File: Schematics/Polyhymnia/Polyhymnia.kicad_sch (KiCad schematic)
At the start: 1 part, among them U1 Teensy4.1

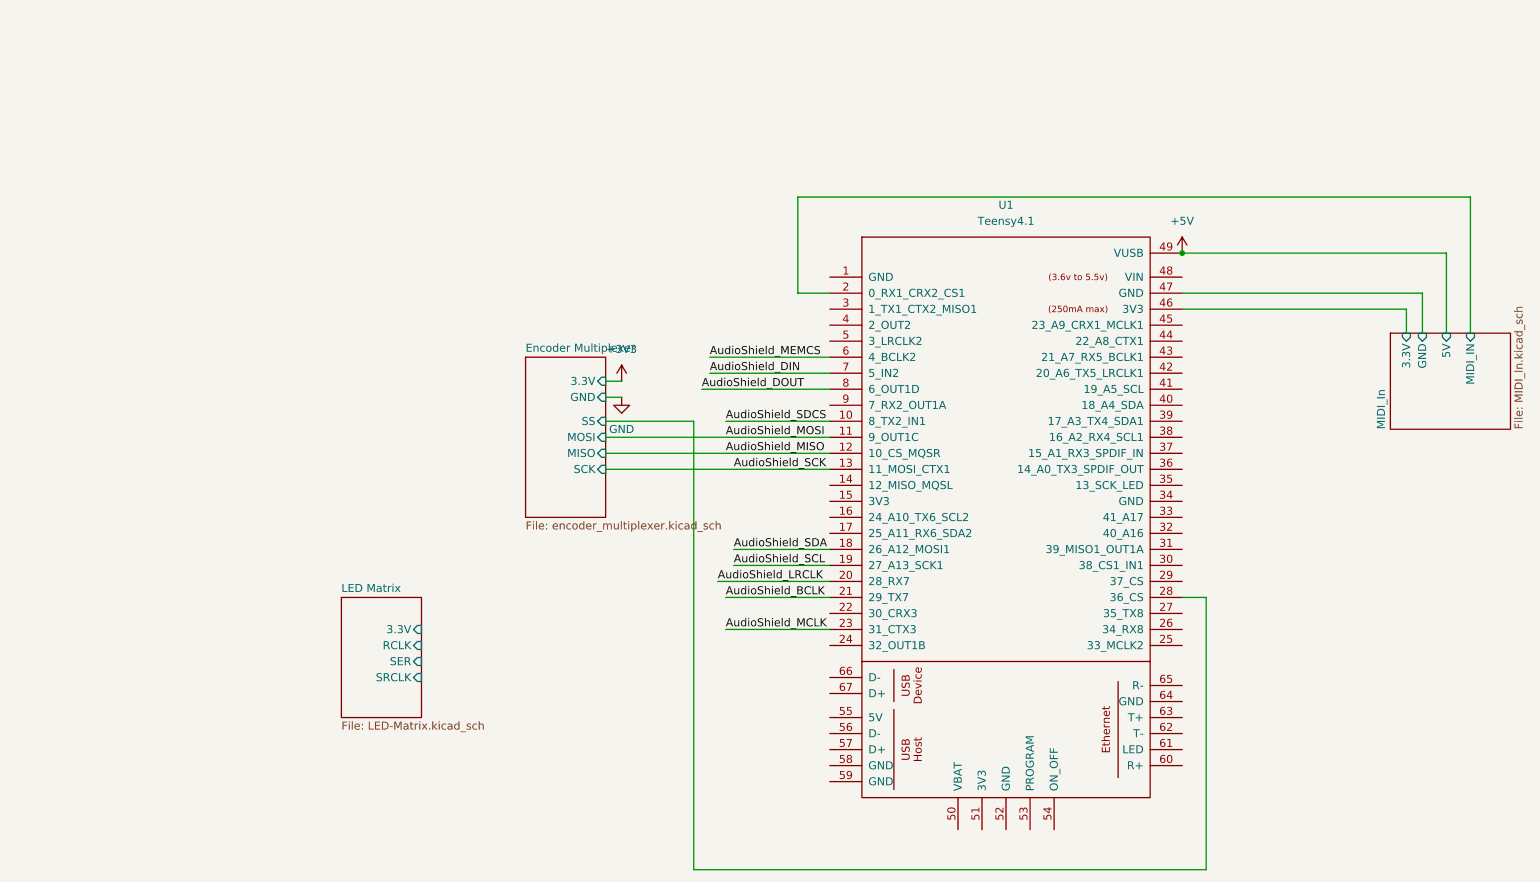
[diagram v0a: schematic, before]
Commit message: Added audio amplifier schematics
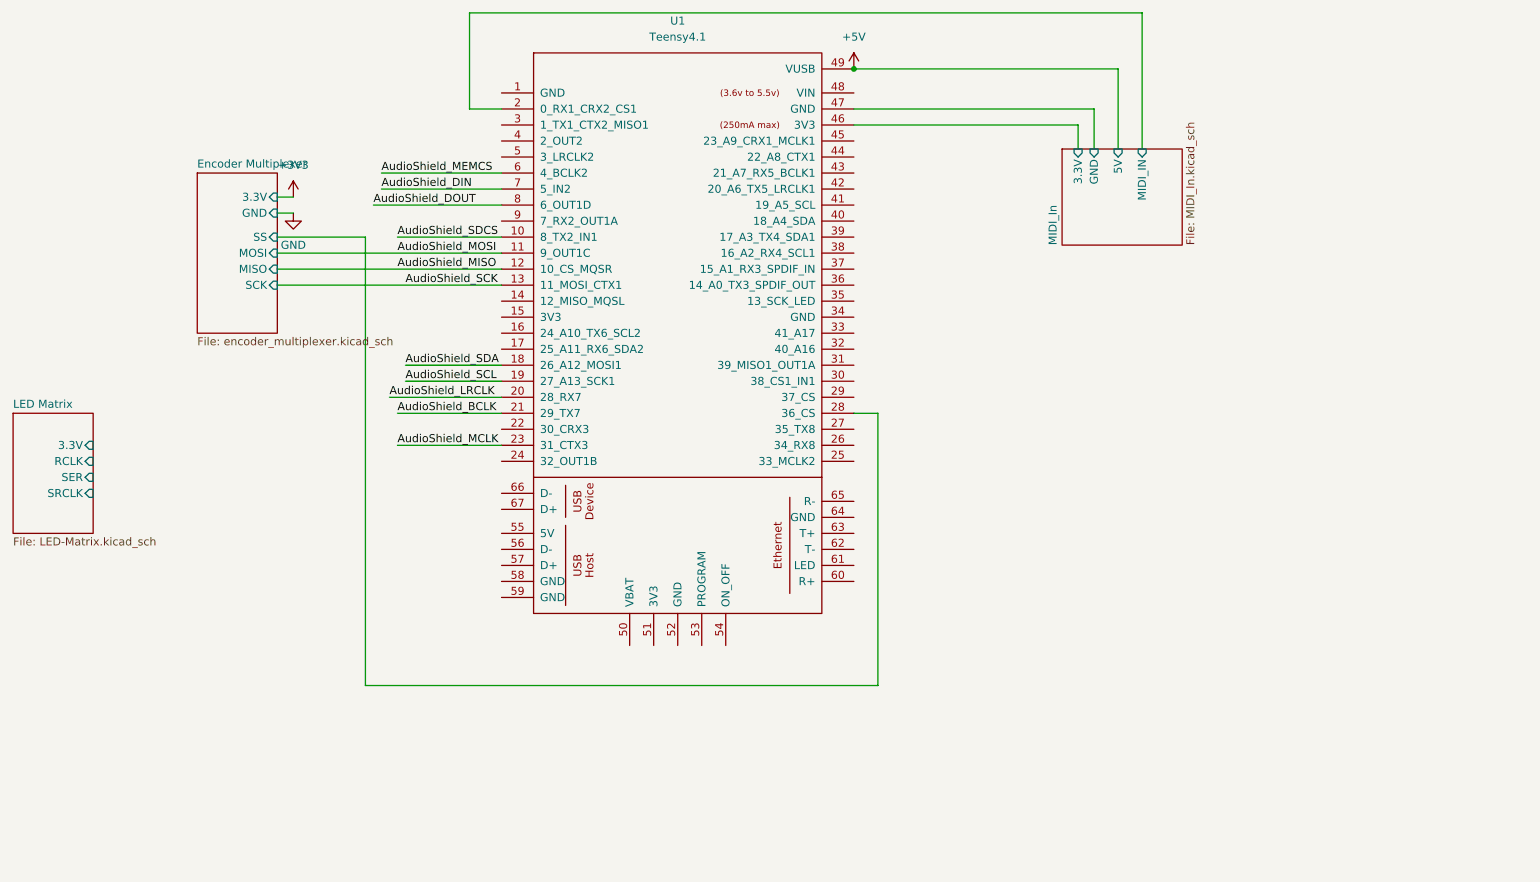
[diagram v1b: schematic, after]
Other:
- title: Polyhymnia -> Polyhymnia Main
- moved on the sheet: U1
